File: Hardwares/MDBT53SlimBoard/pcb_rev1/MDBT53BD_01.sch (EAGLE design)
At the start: 46 parts, among them CN1 USB4105-GF-A, CN2 IF_6PIN, CN3 51296-0894, Q1 BSS84AKQBZ, SW1 SKRPACE010, SW2 SKTADAE010, U2 XC6206P302MR-G, U3 RV-3028-C7, X1 FC-135_32.7680KA-AC

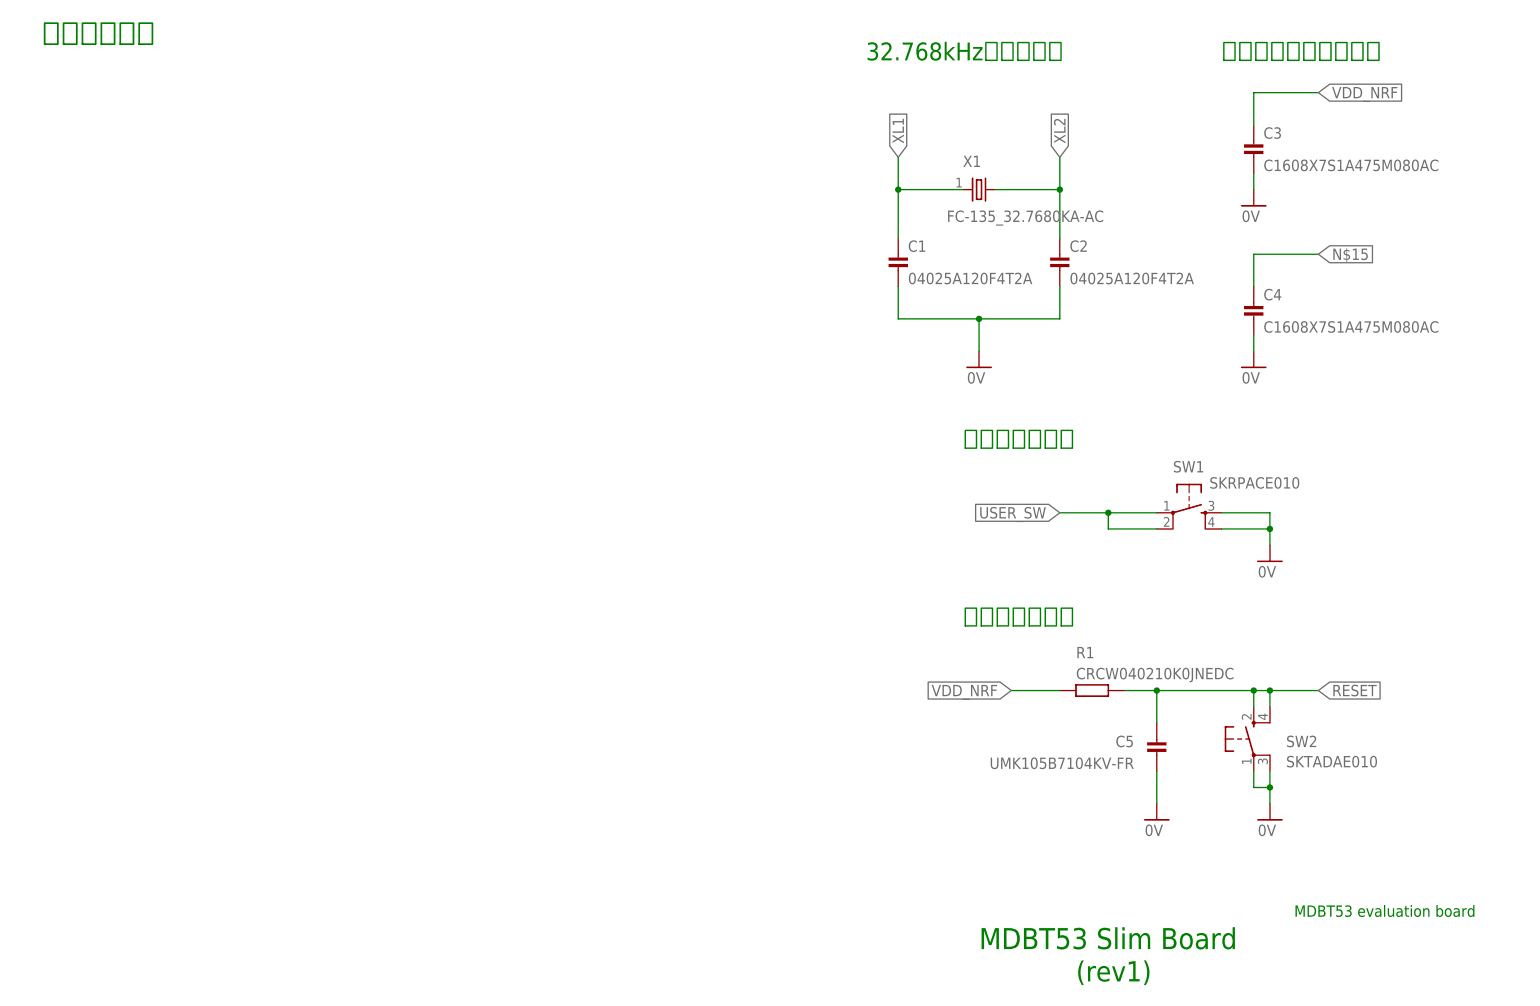
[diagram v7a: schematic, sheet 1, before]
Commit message: 回路図の作成
・MDBT53と接続
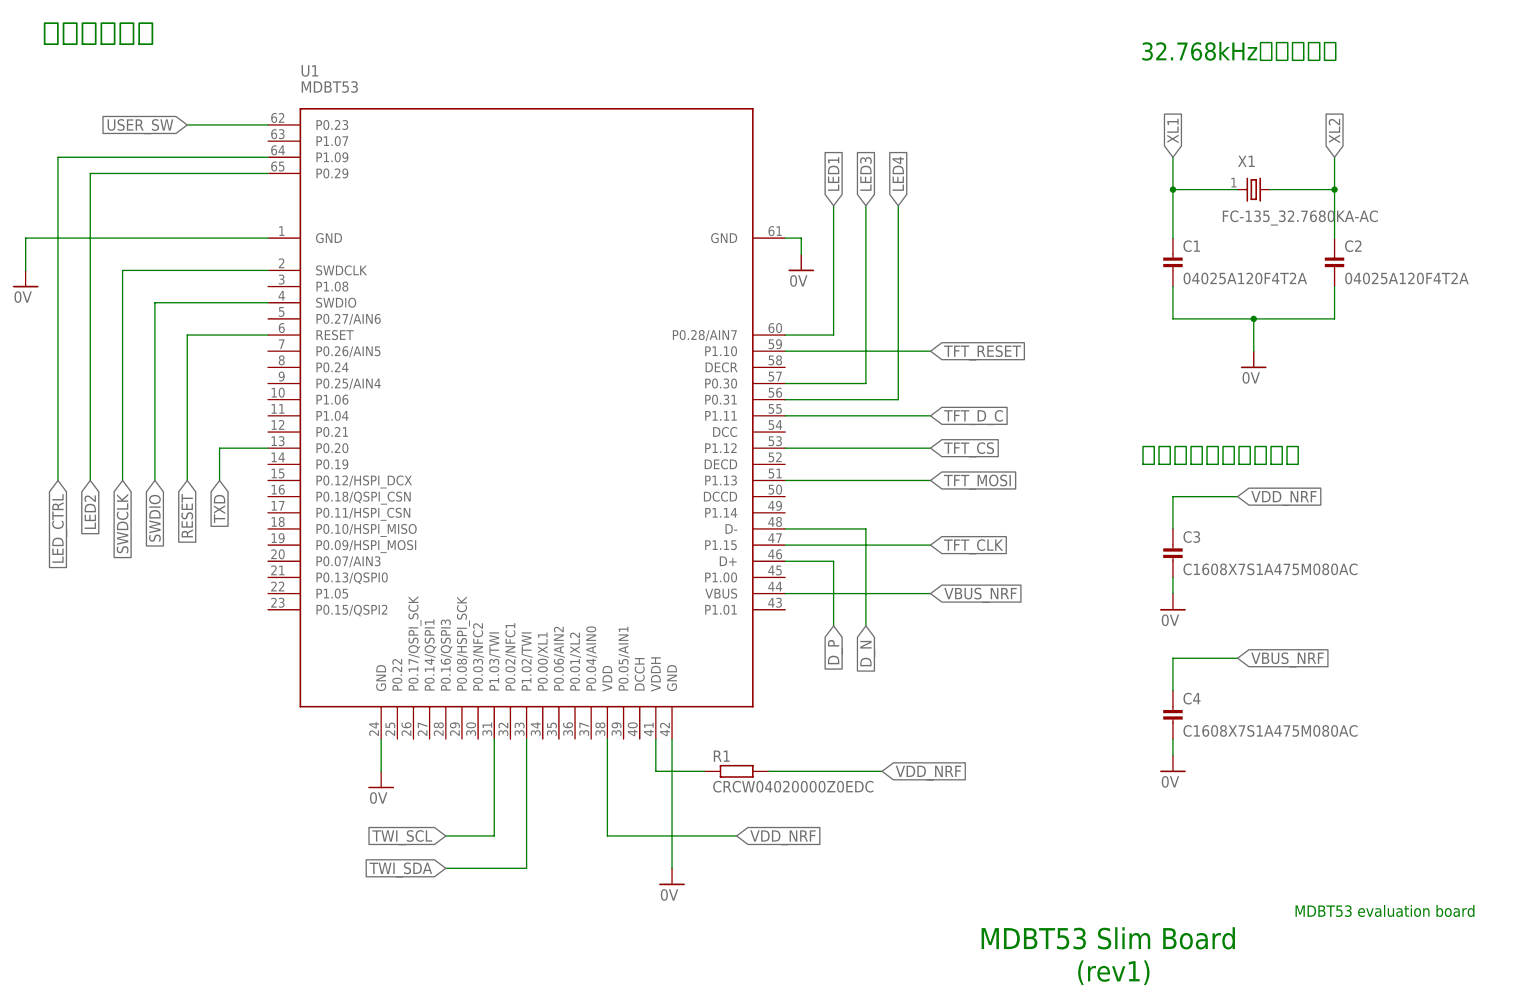
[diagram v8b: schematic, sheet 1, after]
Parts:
- added R14: CRCW040210K0JNEDC, Parts:RESISTOR_0402N
- added U1: MDBT53, Modules:MDBT53
- C11: value TMR107B7105KA-T -> UMK105B7104KV-FR; device Parts:CAP_0603N -> Parts:CAP_0402N
- C12: device Parts:CAP_0402N -> Parts:CAP_0402K
- C5: value UMK105B7104KV-FR -> C0402C103K5RAC7411; device Parts:CAP_0402K -> Parts:CAP_0402N
- C6: value C0402C103K5RAC7411 -> UMK105B7104KV-FR
- C8: value UMK105B7104KV-FR -> C0603C106M8PACTU; device Parts:CAP_0402N -> Parts:CAP_0603N
- C9: value C0603C106M8PACTU -> TMR107B7105KA-T
- R1: value CRCW040210K0JNEDC -> CRCW04020000Z0EDC
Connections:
- net 0V: now also U1.GND@1, U1.GND@24, U1.GND@42, U1.GND@61
- net D_N: now also U1.D-
- net D_P: now also U1.D+
- net LED1: now also U1.P0.28/AIN7
- net LED2: now also U1.P0.29
- net LED3: now also U1.P0.30
- net LED4: now also U1.P0.31
- net LED_CTRL: now also U1.P1.09
- net N$15: now also R1.1, U1.VDDH; no longer C4.1
- net N$17: now also C5.1, C7.1; no longer C6.1, C9.1
- net N$8: now also C10.1; no longer C11.1
- net RESET: now also C12.1, R14.2, U1.RESET; no longer C5.1, R1.2
- net SWDCLK: now also U1.SWDCLK
- net SWDIO: now also U1.SWDIO
- net TFT_CLK: now also U1.P1.15
- net TFT_CS: now also U1.P1.12
- net TFT_D_C: now also U1.P1.11
- net TFT_MOSI: now also U1.P1.13
- net TFT_RESET: now also U1.P1.10
- net TWI_SCL: now also U1.P1.03/TWI
- net TWI_SDA: now also U1.P1.02/TWI
- net TXD: now also U1.P0.20
- net USER_SW: now also U1.P0.23
- net VBUS_LDO: now also C9.1; no longer C10.1
- net VBUS_NRF: now also C4.1, C6.1, U1.VBUS; no longer C7.1
- net VDD_NRF: now also C11.1, R1.2, R14.1, U1.VDD; no longer C12.1, R1.1
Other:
- moved on the sheet: C1, C10, C2, C3, C4, C6, C7, C8, C9, CN3, Q1, R1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
